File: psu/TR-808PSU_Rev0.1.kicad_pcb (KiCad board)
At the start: 2 copper layers, 142.9 x 119.4 mm, 67 parts, among them IC1 uA7805, IC2 TA7179P, P1 1, P10 10, P11 11, P12 12, P13 13, P14 14, P15 15, P16 16, P17 17, P18 18, P19 19, P2 2, P20 20, P21 21, P22 22, P3 3, P4 4, P5 5, P6 6, P7 7, P8 8, P9 9, Q1 2SB596, Q2 2SD880

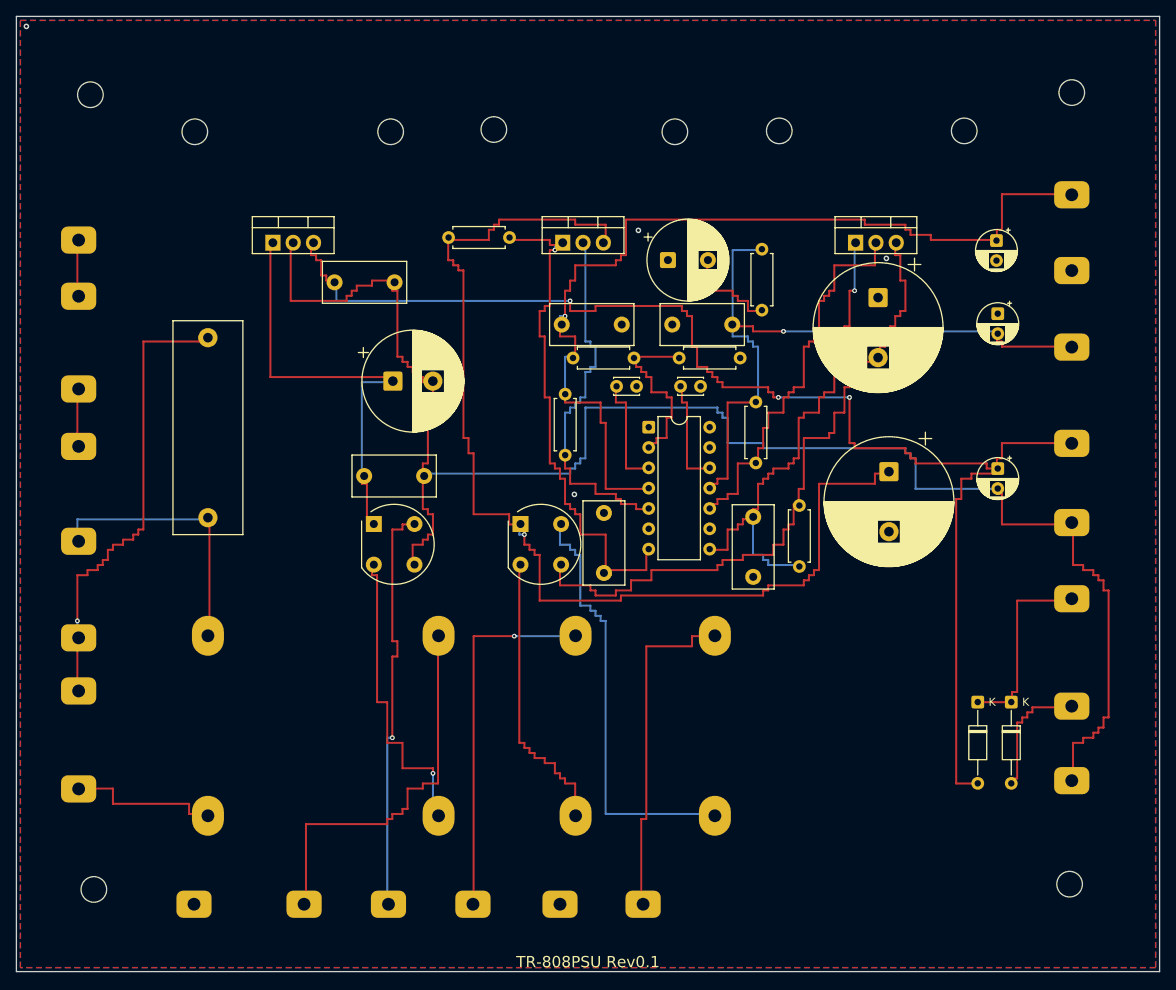
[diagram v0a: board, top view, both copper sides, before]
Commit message: Bahnen am Original-Kupfer geführt: Scan-Abgleich und Leitkarte
Kupfermaske aus dem Halbtonscan, Bauteile am Kupfer ausgerichtet, Router mit
Kostenkarte aus den Netzgebieten des Originals. 56 % der Bahnlänge im
Original-Kupfer, DRC ohne Fehler, keine offenen Verbindungen.

Co-Authored-By: Claude Sonnet 5.5 <noreply@anthropic.com>
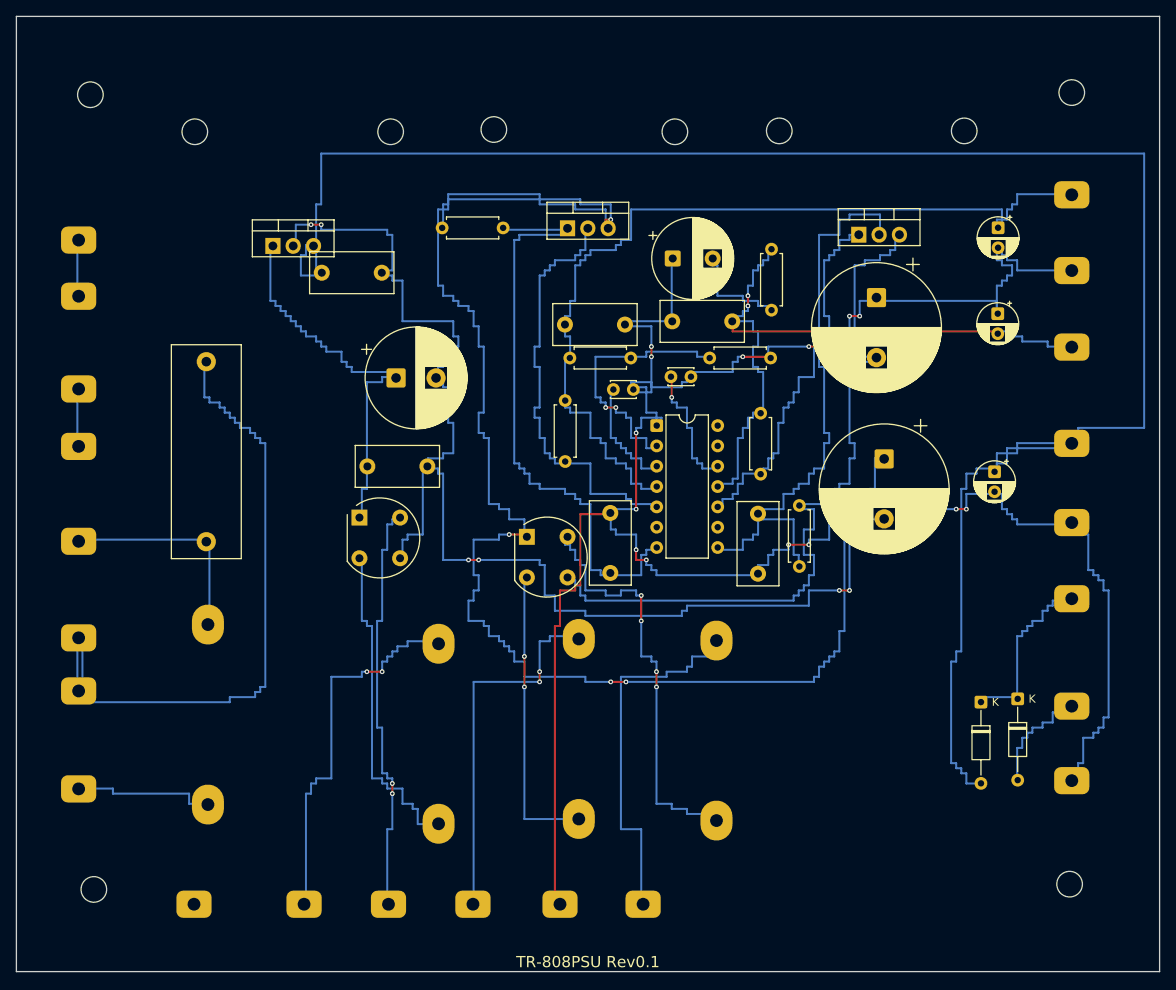
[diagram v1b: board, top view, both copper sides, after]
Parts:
- moved R4 3.81 mm to (86.7, 42.7)
- moved C1 3.01 mm to (23.7, 65.7)
- moved C2 2.00 mm to (38.2, 32.0)
- moved D1 1.97 mm to (42.9, 62.6)
- moved Q1 1.90 mm to (68.9, 26.5)
- moved D2 1.79 mm to (63.8, 65.0)
- moved C13 1.71 mm to (108.5, 55.3)
- moved C8 1.70 mm to (81.8, 45.0)
- moved C14 1.61 mm to (122.7, 26.4)
- moved R5 1.52 mm to (93.0, 57.2)
- moved R7 1.44 mm to (53.2, 26.4)
- moved F1 1.40 mm to (23.9, 76.0)
- moved C4 1.26 mm to (43.9, 56.2)
- moved R6 1.20 mm to (94.4, 36.7)
- moved Q2 1.08 mm to (105.3, 27.3)
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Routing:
- net /GND15: track 0.00 -> 254.5 mm, vias 4 -> 15
- net /RAW15P: track 143.2 -> 217.8 mm, vias 1 -> 4
- net /+5V: track 176.4 -> 250.6 mm, vias 3 -> 0
- net /SW_B: track 61.9 -> 89.9 mm, vias 1 -> 0
- net /GND5: track 216.5 -> 241.8 mm, vias 0 -> 8
- net /RAW15N: track 93.5 -> 104.9 mm
- net /ADJ: track 25.4 -> 35.2 mm, vias 0 -> 2
- net /COL1: track 49.4 -> 58.9 mm
- net /VB1: track 70.7 -> 79.9 mm, vias 1 -> 0
- net /SW_A: track 34.7 -> 28.5 mm
- net /COL2: track 55.2 -> 60.7 mm
- net /AC15_RAW_B: track 43.1 -> 48.0 mm
- net /COMP2: track 13.8 -> 17.5 mm, vias 0 -> 1
- net /VB2: track 69.7 -> 73.2 mm, vias 1 -> 0
- net Net-(D1-Pad2): track 39.8 -> 43.0 mm, vias 1 -> 0
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- removed copper zone on B.Cu, net /GND15
- removed copper zone on F.Cu, net /GND15

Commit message: Breite Bahnen (1,0 mm) und geglättet mit pcb-glaetten
Alle Netze breit verlegt (GND5, GND15, COL1 schmal), Via-Kosten hoch, danach
Treppen zu 45-Grad-Zuegen und Boegen. DRC ohne Fehler, 0 offen, Netzabstand 7,9 mm.

Co-Authored-By: Claude Sonnet 5.5 <noreply@anthropic.com>
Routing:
- net /+5V: track 250.6 -> 183.6 mm
- net /RAW15P: track 217.8 -> 157.2 mm, vias 4 -> 2
- net /GND5: track 241.8 -> 197.2 mm, vias 8 -> 3
- net /GND15: track 254.5 -> 216.1 mm, vias 15 -> 2
- net /-15V: track 93.6 -> 112.7 mm, vias 2 -> 0
- net /RAW15N: track 104.9 -> 86.7 mm
- net /VB2: track 73.2 -> 56.7 mm
- net /VB1: track 79.9 -> 64.2 mm
- net /+15V: track 121.7 -> 108.4 mm
- net /AC15_B: track 56.5 -> 43.7 mm, vias 4 -> 0
- net /COL1: track 58.9 -> 47.5 mm
- net /COL2: track 60.7 -> 50.6 mm
- net /AC15_RAW_B: track 48.0 -> 38.0 mm
- net /RAW5: track 56.2 -> 46.5 mm
- net /AC15_RAW_A: track 48.1 -> 38.9 mm, vias 2 -> 0
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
